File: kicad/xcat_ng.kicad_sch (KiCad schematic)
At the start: 23 parts, among them J1 Conn_01x22, J2 Pico, J3 Conn_02x06_Odd_Even, Q1 BSS138, Q2 BSS138, Q3 BSS138, Q4 BSS138, U1 SN74LV244APWR, U2 SN74LV244APWR, U3 SN74LV244APWR

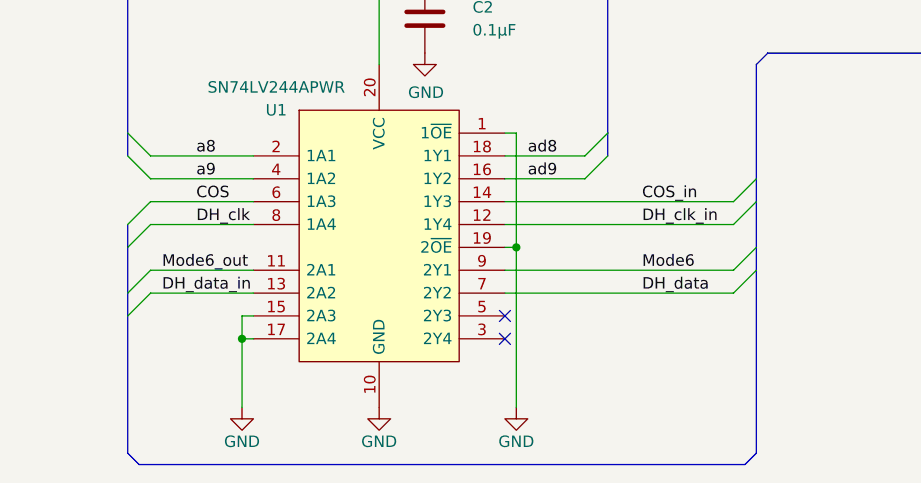
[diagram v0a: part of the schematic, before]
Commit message: Fixed DH_data_in / DH_data, they were swapped at the level converter.
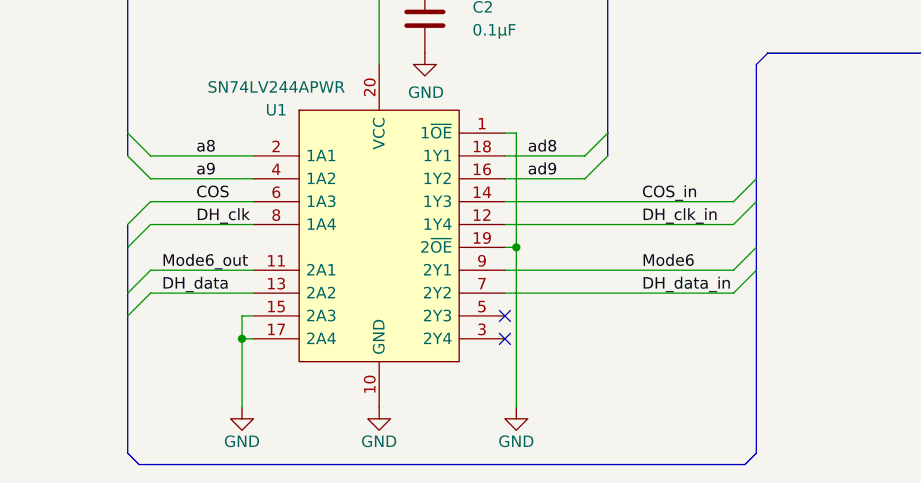
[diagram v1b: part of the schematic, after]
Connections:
- net DH_data: now also U1.13 (2A2); no longer U1.7 (2Y2)
- net DH_data_in: now also U1.7 (2Y2); no longer U1.13 (2A2)
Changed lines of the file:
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@@
     (title "Xcat NG for Syntor X")
     (date "2022-08-12")
-    (rev "0")
+    (rev "B")
     (company "Xcat group https://groups.io/g/xcat/topics")
     (comment 2 "PCB: WA1JHK")
@@
     (effects (font (size 1.27 1.27)) (justify left bottom))
   )
-  (label "DH_data_in" (at 64.77 179.07 0)
+  (label "DH_data" (at 64.77 179.07 0)
     (effects (font (size 1.27 1.27)) (justify left bottom))
   )
@@
     (effects (font (size 1.27 1.27)) (justify left bottom))
   )
-  (label "DH_data" (at 118.11 179.07 0)
-    (effects (font (size 1.27 1.27)) (justify left bottom))
-  )
+  (label "DH_data_in" (at 118.11 179.07 0)
+    (effects (font (size 1.27 1.27)) (justify left bottom))
+  )
